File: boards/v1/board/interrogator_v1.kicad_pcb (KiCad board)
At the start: 2 copper layers, 67.9 x 39.9 mm, 330 parts

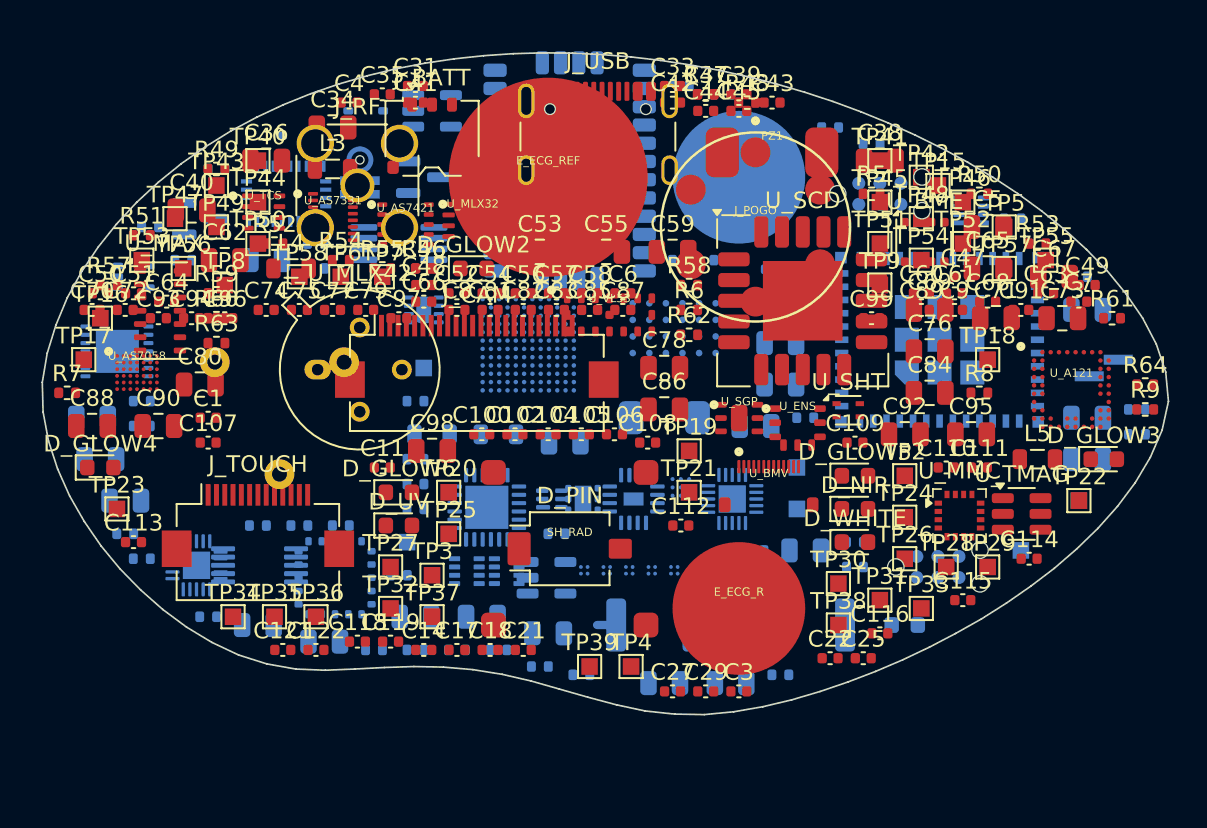
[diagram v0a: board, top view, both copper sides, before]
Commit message: H3.1R/H3.2R: board-first minimal floorplan (ADR-0004) — bean containment removed, board rebuilt placement-true
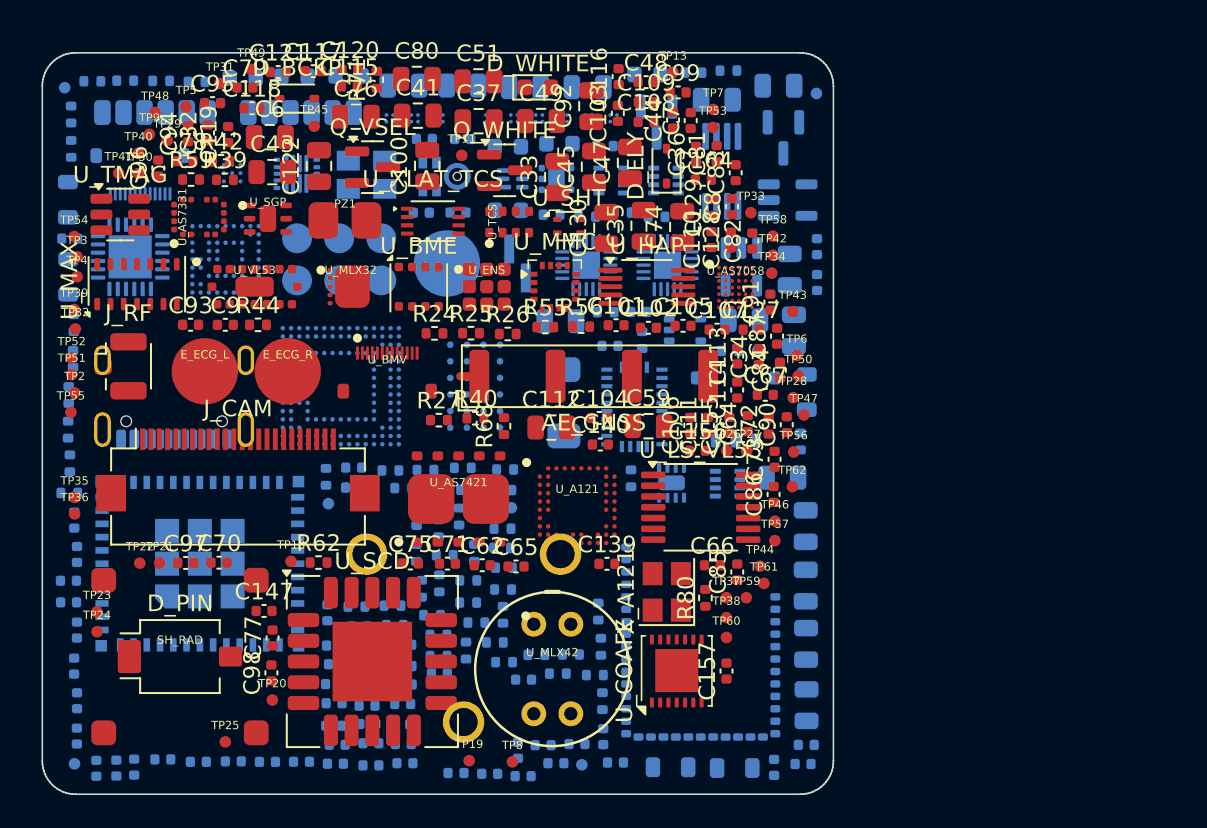
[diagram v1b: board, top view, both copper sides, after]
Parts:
- removed D_NIR: LED_0603_1608Metric, LED_0603_1608Metric
- removed the E_ECG_L at (42.0, 7.50)
- removed the E_ECG_R at (42.0, 33.5)
- removed the E_ECG_REF at (30.5, 7.50)
- removed the J_POGO at (43.0, 10.5)
- removed the J_RF at (19.0, 8.00)
- removed the J_SWD_BL at (50.5, 8.50)
- removed the J_TOUCH at (13.0, 28.5)
- removed the U_CHG at (35.6, 26.9)
- added C124: C_0402_1005Metric, C_0402_1005Metric, B.Cu at (19.1, 34.6)
- added C125: C_0402_1005Metric, C_0402_1005Metric, B.Cu at (21.8, 35.7)
- added C126: C_0402_1005Metric, C_0402_1005Metric, B.Cu at (19.7, 35.6)
- added C127: C_0402_1005Metric, C_0402_1005Metric, F.Cu at (42.7, 16.7)
- added C128: C_0402_1005Metric, C_0402_1005Metric, F.Cu at (41.5, 11.3)
- added C129: C_0402_1005Metric, C_0402_1005Metric, F.Cu at (40.4, 9.33)
- added C130: C_0805_2012Metric, C_0805_2012Metric, F.Cu at (34.0, 10.6)
- added C131: C_0402_1005Metric, C_0402_1005Metric, B.Cu at (21.8, 37.0)
- added C132: C_0402_1005Metric, C_0402_1005Metric, B.Cu at (23.9, 37.4)
- added C133: C_0805_2012Metric, C_0805_2012Metric, B.Cu at (31.2, 16.2)
- added C134: C_0402_1005Metric, C_0402_1005Metric, B.Cu at (17.6, 35.7)
- added C135: C_0402_1005Metric, C_0402_1005Metric, B.Cu at (19.8, 36.9)
- added C136: C_0402_1005Metric, C_0402_1005Metric, B.Cu at (21.8, 38.1)
- added C137: C_0402_1005Metric, C_0402_1005Metric, B.Cu at (17.7, 36.9)
- added C138: C_0805_2012Metric, C_0805_2012Metric, B.Cu at (29.1, 2.07)
- added C139: C_0402_1005Metric, C_0402_1005Metric, F.Cu at (34.0, 30.8)
- added C140: C_0402_1005Metric, C_0402_1005Metric, F.Cu at (33.6, 23.6)
- added C141: C_0402_1005Metric, C_0402_1005Metric, B.Cu at (1.93, 28.2)
- added C142: C_0805_2012Metric, C_0805_2012Metric, B.Cu at (25.3, 1.97)
- added C143: C_0402_1005Metric, C_0402_1005Metric, B.Cu at (2.09, 30.2)
- added C144: C_0402_1005Metric, C_0402_1005Metric, B.Cu at (19.7, 38.1)
- added C145: C_0402_1005Metric, C_0402_1005Metric, B.Cu at (21.7, 39.3)
- added C146: C_0402_1005Metric, C_0402_1005Metric, B.Cu at (17.6, 38.1)
- added C147: C_0402_1005Metric, C_0402_1005Metric, F.Cu at (13.4, 33.6)
- added C148: C_0402_1005Metric, C_0402_1005Metric, B.Cu at (30.2, 41.7)
- added C149: C_0402_1005Metric, C_0402_1005Metric, B.Cu at (32.2, 41.7)
- added C150: C_0402_1005Metric, C_0402_1005Metric, B.Cu at (19.6, 39.4)
- added C151: C_0402_1005Metric, C_0402_1005Metric, B.Cu at (21.7, 40.5)
- added C152: C_0402_1005Metric, C_0402_1005Metric, B.Cu at (17.6, 39.2)
- added C153: C_0402_1005Metric, C_0402_1005Metric, B.Cu at (34.6, 42.8)
- added C154: C_0402_1005Metric, C_0402_1005Metric, B.Cu at (19.6, 40.5)
- added C155: C_0402_1005Metric, C_0402_1005Metric, F.Cu at (41.4, 22.5)
- added C156: C_0402_1005Metric, C_0402_1005Metric, F.Cu at (39.5, 24.0)
- added C157: C_0402_1005Metric, C_0402_1005Metric, F.Cu at (41.3, 37.3)
- added C158: C_0402_1005Metric, C_0402_1005Metric, B.Cu at (28.7, 42.1)
- added C159: C_0402_1005Metric, C_0402_1005Metric, B.Cu at (46.7, 13.8)
- added C160: C_0402_1005Metric, C_0402_1005Metric, B.Cu at (31.0, 42.8)
- added C161: C_0402_1005Metric, C_0402_1005Metric, B.Cu at (21.8, 41.7)
- added C162: C_0402_1005Metric, C_0402_1005Metric, B.Cu at (17.6, 40.6)
- added C163: C_0402_1005Metric, C_0402_1005Metric, B.Cu at (46.7, 11.7)
- added C164: C_0402_1005Metric, C_0402_1005Metric, F.Cu at (39.9, 7.65)
- added E_ECG_L: ELECTRODE_LAND_4MM, ELECTRODE_LAND_4MM, F.Cu at (9.80, 19.2)
- added E_ECG_R: ELECTRODE_LAND_4MM, ELECTRODE_LAND_4MM, F.Cu at (14.8, 19.2)
- added E_ECG_REF: ELECTRODE_LAND_4MM, ELECTRODE_LAND_4MM, B.Cu at (24.4, 12.7)
- added J_POGO: POGO6_COMPACT, POGO6_COMPACT, B.Cu at (17.9, 12.4)
- added J_RF: U.FL_Hirose_U.FL-R-SMT-1_Vertical, U.FL_Hirose_U.FL-R-SMT-1_Vertical, F.Cu at (4.72, 18.9)
- added J_SWD_BL: SWD_PADROW_6, SWD_PADROW_6, B.Cu at (15.6, 3.60)
- added J_TOUCH: ZIF13_MOLEX_503566, ZIF13_MOLEX_503566, B.Cu at (5.90, 7.10)
- added Q_VSEL: SOT-23, SOT-23, F.Cu at (19.9, 6.89)
- added R65: R_0402_1005Metric, R_0402_1005Metric, B.Cu at (33.7, 35.8)
- added R66: R_0402_1005Metric, R_0402_1005Metric, B.Cu at (31.9, 36.3)
- added R67: R_0402_1005Metric, R_0402_1005Metric, B.Cu at (29.8, 36.3)
- added R68: R_0402_1005Metric, R_0402_1005Metric, F.Cu at (27.8, 22.5)
- added R69: R_0402_1005Metric, R_0402_1005Metric, B.Cu at (3.02, 1.71)
- added R70: R_0402_1005Metric, R_0402_1005Metric, B.Cu at (33.3, 37.5)
- added R71: R_0402_1005Metric, R_0402_1005Metric, F.Cu at (20.2, 1.62)
- added R72: R_0402_1005Metric, R_0402_1005Metric, B.Cu at (18.9, 33.4)
- added R73: R_0402_1005Metric, R_0402_1005Metric, B.Cu at (27.3, 35.5)
- added R74: R_0402_1005Metric, R_0402_1005Metric, B.Cu at (31.1, 37.4)
- added R75: R_0402_1005Metric, R_0402_1005Metric, B.Cu at (23.9, 35.1)
- added R76: R_0402_1005Metric, R_0402_1005Metric, B.Cu at (27.8, 36.7)
- added R77: R_0402_1005Metric, R_0402_1005Metric, B.Cu at (21.3, 34.5)
- added R78: R_0402_1005Metric, R_0402_1005Metric, B.Cu at (35.5, 25.7)
- added R79: R_0402_1005Metric, R_0402_1005Metric, B.Cu at (33.8, 39.1)
- added R80: R_0402_1005Metric, R_0402_1005Metric, F.Cu at (40.0, 32.9)
- added R81: R_0402_1005Metric, R_0402_1005Metric, B.Cu at (25.5, 36.0)
- added R82: R_0402_1005Metric, R_0402_1005Metric, B.Cu at (23.9, 36.4)
- added TP59: TESTPOINT_PAD_0.8MM, TESTPOINT_PAD_0.8MM, F.Cu at (42.5, 32.9)
- added TP60: TESTPOINT_PAD_0.8MM, TESTPOINT_PAD_0.8MM, F.Cu at (41.2, 35.2)
- added TP61: TESTPOINT_PAD_0.8MM, TESTPOINT_PAD_0.8MM, F.Cu at (43.5, 32.0)
- added TP62: TESTPOINT_PAD_0.8MM, TESTPOINT_PAD_0.8MM, F.Cu at (45.2, 26.2)
- added U_CHG: BQ25620_WQFN18_RYK, BQ25620_WQFN18_RYK, B.Cu at (15.3, 7.30)
- added U_LS_VL53: TSSOP-14_4.4x5mm_P0.65mm, TSSOP-14_4.4x5mm_P0.65mm, F.Cu at (39.7, 27.4)
- added U_SW1V8_AIR: TPS22916_CSP4, TPS22916_CSP4, B.Cu at (34.5, 3.95)
- added U_SW1V8_OPTICAL: TPS22916_CSP4, TPS22916_CSP4, B.Cu at (31.4, 3.95)
- added U_SW1V8_RADAR: TPS22916_CSP4, TPS22916_CSP4, B.Cu at (33.0, 3.95)
- added U_XLAT_TCS: VSSOP-8_2.4x2.1mm_P0.5mm, VSSOP-8_2.4x2.1mm_P0.5mm, F.Cu at (23.6, 10.1)
- added X_A121: Crystal_SMD_3225-4Pin_3.2x2.5mm, Crystal_SMD_3225-4Pin_3.2x2.5mm, F.Cu at (37.7, 32.5)
- added X_HSE: Crystal_SMD_3225-4Pin_3.2x2.5mm, Crystal_SMD_3225-4Pin_3.2x2.5mm, B.Cu at (19.5, 7.35)
- AE_GNSS, D_BCKP, D_FLY, Q_WHITE, R24, R25, R26, R27, R39, R40, R42, R44, U_COAFE, U_HAP: moved to F.Cu
- C1, C11, C14, C22, C27, C3, C4, C42, C46, C50, C52, C54, C56, C57, C58, C60, C61, C63, C68, C89, D_GLOW2, D_GLOW3, D_GLOW4, D_GLOW5, D_GLOW6, D_UV, J_BATT, J_USB, L3, L4, L5, R47, R48, R49, R5, R50, R51, R52, R53, R54, R57, R58, R6, R60, R61, R63, R64, R7, R8, R9: moved to B.Cu
- C100, C112, C122, C33, C35, C37, C41, C43, C45, C47, C49, C51, C6, C74: value C_0402_1005Metric -> C_0805_2012Metric; footprint C_0402_1005Metric -> C_0805_2012Metric
- C101, C103, C117, C120, C32: value C_0805_2012Metric -> C_0402_1005Metric; footprint C_0805_2012Metric -> C_0402_1005Metric; moved to F.Cu
- C12, C123, C13, C16, C19, C2, C23, C26, C30, C34, C36, C62, C65, C67, C71, C73, C78, C84, C86, C90, C95, C98: value C_0805_2012Metric -> C_0402_1005Metric; footprint C_0805_2012Metric -> C_0402_1005Metric
- C17, C18, C21, C25, C29, C31, C39: value C_0402_1005Metric -> C_0805_2012Metric; footprint C_0402_1005Metric -> C_0805_2012Metric; moved to B.Cu
- C38, C40, C5, C53, C55, C69, C88: value C_0805_2012Metric -> C_0402_1005Metric; footprint C_0805_2012Metric -> C_0402_1005Metric; moved to B.Cu
- J_SWD_N6: value Tag-Connect_TC2030-IDC-NL_2x03_P1.27mm_Vertical -> SWD_PADROW_6; footprint Tag-Connect_TC2030-IDC-NL_2x03_P1.27mm_Vertical -> SWD_PADROW_6
- TP1, TP10, TP12, TP14, TP18, TP19, TP2, TP20, TP21, TP22, TP23, TP24, TP25, TP26, TP27, TP28, TP29, TP3, TP30, TP31, TP32, TP33, TP34, TP35, TP36, TP37, TP38, TP39, TP4, TP40, TP41, TP42, TP43, TP44, TP45, TP46, TP47, TP48, TP49, TP5, TP50, TP51, TP52, TP53, TP54, TP55, TP56, TP57, TP58, TP6, TP7, TP8, TP9: value TestPoint_Pad_1.0x1.0mm -> TESTPOINT_PAD_0.8MM; footprint TestPoint_Pad_1.0x1.0mm -> TESTPOINT_PAD_0.8MM
- TP11, TP13: value TestPoint_Pad_1.0x1.0mm -> TESTPOINT_PAD_0.8MM; footprint TestPoint_Pad_1.0x1.0mm -> TESTPOINT_PAD_0.8MM; moved to F.Cu
- TP15, TP16, TP17: value TestPoint_Pad_1.0x1.0mm -> TESTPOINT_PAD_0.8MM; footprint TestPoint_Pad_1.0x1.0mm -> TESTPOINT_PAD_0.8MM; moved to B.Cu
- U_MLX32: value MLX90632_SFN8_3x3 -> MLX90632_SFN5_3x3; footprint MLX90632_SFN8_3x3 -> MLX90632_SFN5_3x3
- U_MLX42: value TO-39-4 -> MLX90642_TO39; footprint TO-39-4 -> MLX90642_TO39
- U_N657: value ST_VFBGA142_PLACEHOLDER -> ST_VFBGA142; footprint ST_VFBGA142_PLACEHOLDER -> ST_VFBGA142
- moved R9 65.1 mm to (1.63, 26.5)
- moved R61 63.3 mm to (1.56, 22.7), turned to -90 degrees
- moved C16 61.9 mm to (1.58, 31.8)
- moved TP55 59.5 mm to (1.72, 21.7)
- moved L5 59.5 mm to (1.56, 13.5), turned to -90 degrees
- moved C61 59.1 mm to (3.26, 43.1), turned to -90 degrees
- moved R53 59.1 mm to (1.59, 20.6), turned to -90 degrees
- moved TP14 58.5 mm to (1.94, 42.9)
- moved C60 57.5 mm to (2.08, 41.2), turned to -90 degrees
- moved C5 57.5 mm to (9.41, 42.7)
- moved U_TMAG 57.3 mm to (4.70, 9.75)
- moved TP22 56.7 mm to (5.88, 30.8)
- moved TP29 55.8 mm to (7.53, 5.28)
- moved R8 55.0 mm to (1.66, 24.7), turned to -90 degrees
- moved J_SWD_N6 54.6 mm to (6.80, 3.60)
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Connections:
- C1 pad 1: VBUS_C -> PD_VDDD
- C10 pad 1: VSYS -> N$8
- C100 pad 1: 3V3_RADAR -> 3V3_CONTACT
- C101 pad 1: 3V3_RADAR -> 3V3_CONTACT
- C102 pad 1: 3V3_GNSS -> 3V3_CONTACT
- C103 pad 1: 3V3_GNSS -> 3V3_CONTACT
- C104 pad 1: GNSS_VBCKP -> 3V3_AIR
- C105 pad 1: 3V3_SYS -> 3V3_AIR
- C106 pad 1: 3V3_AON -> 3V3_AIR
- C107 pad 1: 3V3_AON -> 3V3_AIR
- C108 pad 1: PIN_BIAS -> 1V8_AIR
- C109 pad 1: RAD_VREF -> 1V8_AIR
- C11 pad 1: VBAT -> N$9
- C110 pad 1: RAD_IN -> 3V3_AIR
- C110 pad 2: RAD_ANALOG -> GND
- C111 pad 1: 3V3_SYS -> 3V3_AIR
- C112 pad 1: 3V3_SYS -> 3V3_AIR
- C113 pad 1: RF_IN -> 3V3_AIR
- C113 pad 2: N$24 -> GND
- C114 pad 1: N$25 -> 3V3_AIR
- C115 pad 1: 3V3_SYS -> 1V8_OPTICAL
- C116 pad 1: 3V3_AIR -> 1V8_OPTICAL
- C117 pad 1: 3V3_AIR -> 3V3_OPTICAL
- C118 pad 1: N$29 -> 3V3_OPTICAL
- C118 pad 2: N$30 -> GND
- C119 pad 1: 3V3_AON -> 3V3_OPTICAL
- C12 pad 1: VBAT -> N$11
- C12 pad 2: GND -> N$10
- C120 pad 1: 3V3_AON -> 3V3_OPTICAL
- C121 pad 1: N$31 -> 3V3_OPTICAL
- C122 pad 1: 3V3_AON -> 3V3_OPTICAL
- C123 pad 1: 3V3_AON -> 3V3_SYS
- C14 pad 1: 3V3_AON -> VSYS
- C15 pad 1: 3V3_AON -> VSYS
- C16 pad 1: VSYS -> VBAT
- C17 pad 1: VDD_CORE_N6 -> VBAT
- C18 pad 1: VDD_CORE_N6 -> VSYS
- C19 pad 1: VDD_CORE_N6 -> 3V3_AON
- C2 pad 1: VBUS_C -> PD_VDDD
- C20 pad 1: VSYS -> 3V3_AON
- C21 pad 1: 3V3_SYS -> VSYS
- C22 pad 1: 3V3_SYS -> VDD_CORE_N6
- C23 pad 1: 3V3_SYS -> VDD_CORE_N6
- C24 pad 1: VSYS -> VDD_CORE_N6
- C25 pad 1: 1V8 -> VSYS
- C26 pad 1: 1V8 -> 3V3_SYS
- C27 pad 1: 3V3_OPTICAL -> 3V3_SYS
- C28 pad 1: 3V3_OPTICAL -> 3V3_SYS
- C29 pad 1: 3V3_AIR -> VSYS
- C3 pad 1: PROT_VDD -> PD_VDDD
- C3 pad 2: CELL_N -> GND
- C30 pad 1: 3V3_AIR -> 1V8
- C31 pad 1: 3V3_CONTACT -> 1V8
- C32 pad 1: 3V3_CONTACT -> 3V3_OPTICAL
- C33 pad 1: 3V3_RADAR -> 3V3_OPTICAL
- C34 pad 1: 3V3_RADAR -> 3V3_AIR
- C35 pad 1: 3V3_GNSS -> 3V3_AIR
- C36 pad 1: 3V3_GNSS -> 3V3_CONTACT
- C37 pad 1: 3V3_WIFI -> 3V3_CONTACT
- C38 pad 1: 3V3_WIFI -> 3V3_RADAR
- C39 pad 1: VACC -> 3V3_RADAR
- C4 pad 1: 3V3_AON -> N$1
- C40 pad 1: VACC -> 3V3_GNSS
- C41 pad 1: VDD_CORE_N6 -> 3V3_GNSS
- C42 pad 1: VDD_CORE_N6 -> 3V3_WIFI
- C43 pad 1: 1V8 -> 3V3_WIFI
- C44 pad 1: 1V8 -> 1V8_OPTICAL
- C45 pad 1: 3V3_SYS -> 1V8_OPTICAL
- C46 pad 1: 3V3_SYS -> 1V8_RADAR
- C47 pad 1: 3V3_SYS -> 1V8_RADAR
- C48 pad 1: 3V3_SYS -> 1V8_AIR
- C49 pad 1: 1V8 -> 1V8_AIR
- C5 pad 1: N$8 -> VBUS_C
- C50 pad 1: 1V8 -> VACC
- C51 pad 1: 3V3_AON -> VACC
- C52 pad 1: 3V3_AON -> N6_V08CAP
- C54 pad 1: 3V3_WIFI -> 1V8
- C55 pad 1: 3V3_WIFI -> VDD_CORE_N6
- C56 pad 1: C6_EN -> VDD_CORE_N6
- C57 pad 1: 3V3_OPTICAL -> VDD_CORE_N6
- C58 pad 1: 3V3_OPTICAL -> VDD_CORE_N6
- C59 pad 1: 3V3_OPTICAL -> VDD_CORE_N6
- C6 pad 1: N$9 -> VBUS_C
- C60 pad 1: 3V3_SYS -> 1V8
- C61 pad 1: 3V3_SYS -> 1V8
- C62 pad 1: 3V3_SYS -> 1V8
- C63 pad 1: 3V3_SYS -> 1V8
- C66 pad 1: 3V3_OPTICAL -> 3V3_SYS
- C67 pad 1: 3V3_OPTICAL -> 3V3_SYS
- C68 pad 1: 3V3_OPTICAL -> N6_OSC_IN
- C69 pad 1: 3V3_OPTICAL -> N6_OSC_OUT
- C7 pad 1: N$11 -> PROT_VDD
- C7 pad 2: N$10 -> CELL_N
- C72 pad 1: 3V3_CONTACT -> 3V3_AON
- C73 pad 1: 3V3_CONTACT -> 3V3_AON
- C74 pad 1: 3V3_CONTACT -> 3V3_AON
- C75 pad 1: 3V3_CONTACT -> 3V3_WIFI
- C76 pad 1: 3V3_CONTACT -> 3V3_WIFI
- C77 pad 1: 3V3_AIR -> C6_EN
- C78 pad 1: 3V3_AIR -> 3V3_OPTICAL
- C79 pad 1: 3V3_AIR -> 3V3_OPTICAL
- C8 pad 1: VSYS -> PACKP
- C80 pad 1: 3V3_AIR -> 3V3_OPTICAL
- C81 pad 1: 1V8 -> 1V8_OPTICAL
- C82 pad 1: 3V3_AIR -> 1V8_OPTICAL
- C83 pad 1: 3V3_AIR -> 1V8_OPTICAL
- C84 pad 1: 3V3_AIR -> 3V3_SYS
- C85 pad 1: 3V3_AIR -> 3V3_SYS
- C86 pad 1: 3V3_AIR -> 3V3_SYS
- C87 pad 1: 3V3_OPTICAL -> 3V3_SYS
- C88 pad 1: 3V3_OPTICAL -> BNO_CAP
- C89 pad 1: 3V3_OPTICAL -> ADS_CAP
- C9 pad 1: VSYS -> GAUGE_VDD
- C90 pad 1: 3V3_OPTICAL -> 3V3_SYS
- C91 pad 1: 3V3_OPTICAL -> 3V3_SYS
- C92 pad 1: 3V3_OPTICAL -> 3V3_SYS
- C93 pad 1: 3V3_SYS -> 3V3_OPTICAL
- C94 pad 1: 3V3_SYS -> 3V3_OPTICAL
- C95 pad 1: 3V3_SYS -> 3V3_OPTICAL
- C96 pad 1: 3V3_SYS -> 3V3_OPTICAL
- C97 pad 1: 3V3_AIR -> 1V8
- C98 pad 1: 3V3_AIR -> 1V8
- C99 pad 1: 3V3_RADAR -> 3V3_CONTACT
- J_BATT pad 1: VBAT -> PACKP
- J_BATT pad MP: (no net) -> GND
- J_CAM pad MP: (no net) -> GND
- L2 pad 1: N$15 -> N$16
- L3 pad 1: N$16 -> N$17
- L4 pad 1: N$18 -> N$19
- L5 pad 1: N$20 -> N$21
- Q_FAN pad 1: N$28 -> N$31
- Q_PROT pad 2: N$5 -> N$4
- Q_PROT pad 5: N$6 -> N$5
- Q_UV pad 1: N$26 -> N$29
- Q_WHITE pad 1: N$27 -> N$30
- R1 pad 1: N$1 -> PD_VDDD
- R1 pad 2: GND -> N$2
- R10 pad 1: BATT_NTC -> N$9
- R10 pad 2: GND -> BATT_NTC
- R11 pad 1: VDD_CORE_N6 -> BATT_NTC
- R11 pad 2: N$17 -> GND
- R12 pad 1: N$17 -> N$15
- R13 pad 1: 3V3_SYS -> VDD_CORE_N6
- R13 pad 2: N$19 -> N$18
- R14 pad 1: N$19 -> N$18
- R15 pad 1: 1V8 -> N$18
- R15 pad 2: N$21 -> VSEL_LEG
- R16 pad 1: N$21 -> N6_VCORE_SEL
- R17 pad 1: I2CA_SDA -> 3V3_SYS
- R17 pad 2: 3V3_SYS -> N$20
- R18 pad 1: I2CA_SCL -> N$20
- R18 pad 2: 3V3_SYS -> GND
- R19 pad 1: I2CB_SDA -> 1V8
- R19 pad 2: 3V3_SYS -> N$22
- R20 pad 1: I2CB_SCL -> N$22
- R20 pad 2: 3V3_SYS -> GND
- R21 pad 1: N6_NRST -> N6_PWR_ON
- R21 pad 2: 3V3_SYS -> GND
- R22 pad 1: N6_BOOT0 -> N$23
- R23 pad 1: NOR_RST_N -> N$24
- R23 pad 2: 1V8 -> GND
- R24 pad 1: SENT_SDA -> I2CA_SDA
- R24 pad 2: 3V3_AON -> 3V3_SYS
- R25 pad 1: SENT_SCL -> I2CA_SCL
- R25 pad 2: 3V3_AON -> 3V3_SYS
- R26 pad 1: GAUGE_INT_N -> I2CB_SDA
- R26 pad 2: 3V3_AON -> 3V3_SYS
- R27 pad 1: CHG_INT_N -> I2CB_SCL
- R27 pad 2: 3V3_AON -> 3V3_SYS
- R28 pad 1: PD_FAULT_N -> N6_NRST
- R28 pad 2: 3V3_AON -> 3V3_SYS
- R29 pad 1: BL_RESET_N -> N6_BOOT0
- R29 pad 2: 3V3_AON -> GND
- R3 pad 1: N$3 -> PD_VDDD
- R3 pad 2: GND -> N$3
- R30 pad 1: 3V3_WIFI -> N6_BOOT1
- R30 pad 2: C6_EN -> GND
- R31 pad 1: C6_BOOT -> NOR_RST_N
- R31 pad 2: 3V3_WIFI -> 1V8
- R32 pad 1: INT_VL53 -> SENT_SDA
- R32 pad 2: 3V3_SYS -> 3V3_AON
- R33 pad 1: BNO_PS0_WAKE -> SENT_SCL
- R33 pad 2: 3V3_SYS -> 3V3_AON
- R34 pad 1: INT_BNO -> GAUGE_INT_N
- R34 pad 2: 3V3_SYS -> 3V3_AON
- R35 pad 1: N$22 -> CHG_INT_N
- R35 pad 2: 3V3_SYS -> 3V3_AON
- R36 pad 1: N$23 -> BL_RESET_N
- R36 pad 2: 3V3_SYS -> 3V3_AON
- R37 pad 1: PIEZO_P -> 3V3_WIFI
- R37 pad 2: GND -> C6_EN
- R38 pad 1: PIEZO_N -> C6_BOOT
- R38 pad 2: GND -> 3V3_WIFI
- R39 pad 1: INT_MAX -> VL53_SPI_SEL
- R39 pad 2: 3V3_SYS -> 1V8_OPTICAL
- R4 pad 1: N$4 -> N$3
- R40 pad 1: INT_ENS -> VL53_NCS_1V8
- R40 pad 2: 3V3_SYS -> 1V8_OPTICAL
- R41 pad 1: INT_TCS -> CS_VL53_N
- R42 pad 1: INT_AS7421 -> VL53_GPIO2
- R42 pad 2: 3V3_SYS -> 1V8_OPTICAL
- R43 pad 1: 3V3_OPTICAL -> LPN_VL53
- R43 pad 2: NIR_LED_A -> GND
- R44 pad 1: INT_TMAG -> INT_VL53
- R44 pad 2: 3V3_SYS -> 1V8_OPTICAL
- R45 pad 1: 3V3_AON -> BNO_PS0_WAKE
- R45 pad 2: PIN_BIAS -> 3V3_SYS
- R46 pad 1: 3V3_AON -> INT_BNO
- R46 pad 2: RAD_VREF -> 3V3_SYS
- R47 pad 1: RAD_VREF -> N$25
- R47 pad 2: GND -> 3V3_SYS
- R48 pad 1: RAD_IN -> BNO_ENV_SCL
- R48 pad 2: RAD_ANALOG -> 3V3_SYS
- R49 pad 1: 3V3_AON -> BNO_ENV_SDA
- R49 pad 2: RAD_VTH -> 3V3_SYS
- R5 pad 1: VBAT -> PACKP
- R50 pad 1: RAD_VTH -> N$26
- R50 pad 2: GND -> 3V3_SYS
- R51 pad 1: SHIELD_RAD -> PIEZO_P
- R52 pad 1: 3V3_OPTICAL -> PIEZO_N
- R52 pad 2: UV_LED_A -> GND
- R53 pad 1: UV_GATE -> INT_MAX
- R53 pad 2: N$26 -> 3V3_SYS
- R54 pad 1: 3V3_OPTICAL -> INT_ENS
- R54 pad 2: WHITE_LED_A -> 3V3_SYS
- R55 pad 1: EN_WHITE -> I2CA_SDA_1V8
- R55 pad 2: N$27 -> 1V8_OPTICAL
- R56 pad 1: GLOW1 -> I2CA_SCL_1V8
- R56 pad 2: GLOW1_A -> 1V8_OPTICAL
- R57 pad 1: GLOW2 -> EN_OPTICAL
- R57 pad 2: GLOW2_A -> 3V3_SYS
- R58 pad 1: GLOW3 -> INT_TCS
- R58 pad 2: GLOW3_A -> 3V3_SYS
- R59 pad 1: GLOW4 -> AS7331_REXT
- R59 pad 2: GLOW4_A -> GND
- R6 pad 1: N$7 -> N$6
- R60 pad 1: GLOW5 -> INT_AS7421
- R60 pad 2: GLOW5_A -> 3V3_SYS
- R61 pad 1: GLOW6 -> INT_TMAG
- R61 pad 2: GLOW6_A -> 3V3_SYS
- R62 pad 1: EN_FAN -> 3V3_AON
- R62 pad 2: N$28 -> PIN_BIAS
- R63 pad 1: TOUCH_RDY_N -> 3V3_AON
- R63 pad 2: 3V3_AON -> RAD_VREF
- R64 pad 1: TOUCH_MCLR_N -> RAD_VREF
- R64 pad 2: 3V3_AON -> GND
- R7 pad 1: N$12 (its old number) -> N$7
- R8 pad 2: VBAT -> GND
- R9 pad 1: N$9 -> N$13
- R9 pad 2: BATT_NTC -> VBAT
- TP11 pad 1: VBUS_C -> 1V8_OPTICAL
- TP12 pad 1: VBAT -> 1V8_RADAR
- TP13 pad 1: VSYS -> 1V8_AIR
- TP14 pad 1: 3V3_AON -> VBUS_C
- TP15 pad 1: 3V3_SYS -> VBAT
- TP16 pad 1: VDD_CORE_N6 -> VSYS
- TP17 pad 1: 1V8 -> 3V3_AON
- TP18 pad 1: N6_BOOT0 -> 3V3_SYS
- TP19 pad 1: C6_TXD0 -> VDD_CORE_N6
- TP20 pad 1: C6_RXD0 -> 1V8
- TP21 pad 1: C6_BOOT -> N6_BOOT0
- TP22 pad 1: SPI1_SCK -> N6_BOOT1
- TP23 pad 1: SPI1_MISO -> C6_TXD0
- TP24 pad 1: SPI1_MOSI -> C6_RXD0
- TP25 pad 1: I2CA_SDA -> C6_BOOT
- TP26 pad 1: I2CA_SCL -> SPI1_SCK
- TP27 pad 1: I2CB_SDA -> SPI1_MISO
- TP28 pad 1: I2CB_SCL -> SPI1_MOSI
- TP29 pad 1: SENT_SDA -> I2CA_SDA
- TP3 pad 1: PD_FAULT_N -> PD_FAULT
- TP30 pad 1: SENT_SCL -> I2CA_SCL
- TP31 pad 1: SDIO_CLK -> I2CB_SDA
- TP32 pad 1: SDIO_CMD -> I2CB_SCL
- TP33 pad 1: IMCU_N6_TX -> SENT_SDA
- TP34 pad 1: IMCU_N6_RX -> SENT_SCL
- TP35 pad 1: GNSS_PPS -> SDIO_CLK
- TP36 pad 1: N6_SWDIO -> SDIO_CMD
- TP37 pad 1: N6_SWCLK -> IMCU_N6_TX
- TP38 pad 1: BL_SWDIO -> IMCU_N6_RX
- TP39 pad 1: BL_SWCLK -> GNSS_PPS
- TP40 pad 1: BNO_PS0_WAKE -> N6_SWDIO
- TP41 pad 1: ACC_AN2 -> N6_SWCLK
- TP42 pad 1: CO_AFE_OUT -> BL_SWDIO
- TP43 pad 1: GEIGER_PULSE -> BL_SWCLK
- TP44 pad 1: N6_SWO -> BNO_PS0_WAKE
- TP45 pad 1: BL_SWO -> ACC_AN2
- TP46 pad 1: GND -> CO_AFE_OUT
- TP47 pad 1: USB_DP -> GEIGER_PULSE
- TP48 pad 1: USB_DM -> N6_SWO
- TP49 pad 1: ACC_AN1 -> BL_SWO
- TP50 pad 1: GNSS_TX -> GND
- TP51 pad 1: GNSS_RX -> USB_DP
- TP52 pad 1: RAD_ANALOG -> USB_DM
- TP53 pad 1: RF_DET_OUT -> ACC_AN1
- TP54 pad 1: CLK_ADS -> GNSS_TX
- TP55 pad 1: WAKE_N6 -> GNSS_RX
- TP56 pad 1: ATTN_N6 -> RAD_ANALOG
- TP57 pad 1: EN_N6 -> RF_DET_OUT
- TP58 pad 1: INTERLOCK_OK -> CLK_ADS
- U_1V8 pad 1: EN_N6 -> 3V3_SYS
- U_1V8 pad 3: VSYS -> N$21
- U_1V8 pad 4: N$21 -> VSYS
- U_1V8 pad 5: N$20 -> N$22
- U_A121 pad A2: (no net) -> GND
- U_A121 pad A3: (no net) -> GND
- U_A121 pad A4: (no net) -> GND
- U_A121 pad A5: (no net) -> GND
- U_A121 pad A6: (no net) -> GND
- U_A121 pad A7: (no net) -> GND
- U_A121 pad A8: (no net) -> GND
- U_A121 pad A9: (no net) -> GND
- U_A121 pad B1: (no net) -> GND
- U_A121 pad B10: (no net) -> GND
- U_A121 pad B2: (no net) -> GND
- U_A121 pad B9: (no net) -> GND
- U_A121 pad C1: (no net) -> GND
- U_A121 pad C10: (no net) -> GND
- U_A121 pad C2: (no net) -> 1V8_RADAR
- U_A121 pad C9: (no net) -> 1V8_RADAR
- U_A121 pad D1: (no net) -> 1V8_RADAR
- U_A121 pad D10: (no net) -> 1V8_RADAR
- U_A121 pad D2: (no net) -> GND
- U_A121 pad D9: (no net) -> GND
- U_A121 pad E1: (no net) -> GND
- U_A121 pad E10: (no net) -> GND
- U_A121 pad E2: (no net) -> GND
- U_A121 pad E9: (no net) -> GND
- U_A121 pad F1: (no net) -> GND
- U_A121 pad F10: (no net) -> 3V3_RADAR
- U_A121 pad F2: (no net) -> GND
- U_A121 pad F9: (no net) -> GND
- U_A121 pad G1: (no net) -> GND
- U_A121 pad G10: (no net) -> GND
- U_A121 pad H1: (no net) -> GND
- U_A121 pad H10: (no net) -> A121_XOUT
- U_A121 pad H2: (no net) -> GND
- U_A121 pad H9: (no net) -> GND
- U_A121 pad J1: (no net) -> 3V3_RADAR
- U_A121 pad J10: (no net) -> A121_XIN
- U_A121 pad J2: (no net) -> CS_A121_N
- U_A121 pad J3: (no net) -> GND
- U_A121 pad J5: (no net) -> GND
- U_A121 pad J6: (no net) -> GND
- U_A121 pad J8: (no net) -> GND
- U_A121 pad J9: (no net) -> 1V8_RADAR
- U_A121 pad K2: (no net) -> SPI1_SCK
- U_A121 pad K3: (no net) -> SPI1_MISO
- U_A121 pad K4: (no net) -> GND
- U_A121 pad K5: (no net) -> GND
- U_A121 pad K6: (no net) -> SPI1_MOSI
- U_A121 pad K7: (no net) -> GND
- U_A121 pad K8: (no net) -> IRQ_A121
- U_A121 pad K9: (no net) -> 3V3_RADAR
- U_ADS pad 1: 3V3_SYS -> PIEZO_P
- U_ADS pad 10: GND -> CS_ADS_N
- U_ADS pad 11: CO_AFE_OUT -> DRDY_ADS
- U_ADS pad 12: GND -> SPI1_SCK
- U_ADS pad 13: SPI1_SCK -> SPI1_MISO
- U_ADS pad 15: SPI1_MISO -> CLK_ADS
- U_ADS pad 16: CS_ADS_N -> ADS_CAP
- U_ADS pad 17: DRDY_ADS -> GND
- U_ADS pad 18: N$23 -> 3V3_SYS
- U_ADS pad 19: CLK_ADS -> 3V3_SYS
- U_ADS pad 2: 3V3_SYS -> PIEZO_N
- U_ADS pad 20: (no net) -> GND
- U_ADS pad 21: (no net) -> GND
- U_ADS pad 4: GND -> RAD_ANALOG
- U_ADS pad 5: PIEZO_P -> ACC_AN2
- U_ADS pad 6: PIEZO_N -> GND
- U_ADS pad 7: RAD_ANALOG -> GND
- U_ADS pad 8: GND -> CO_AFE_OUT
- U_ADS pad 9: ACC_AN2 -> N$26
- U_AON pad 1: VSYS -> GND
- U_AON pad 2: GND -> VSYS
- U_AON pad 3: VSYS -> GND
- U_AON pad 4: N$15 -> VSYS
- U_AON pad 5: 3V3_AON -> N$15
- U_AON pad 7: (no net) -> N$16
- U_AON pad 8: (no net) -> 3V3_AON
- U_AS7331 pad 1: 3V3_OPTICAL -> GND
- U_AS7331 pad 10: (no net) -> 3V3_OPTICAL
- U_AS7331 pad 11: (no net) -> GND
- U_AS7331 pad 12: (no net) -> I2CB_SDA
- U_AS7331 pad 13: (no net) -> I2CB_SCL
- U_AS7331 pad 14: (no net) -> GND
- U_AS7331 pad 15: (no net) -> GND
- U_AS7331 pad 16: (no net) -> GND
- U_AS7331 pad 3: I2CB_SDA -> 3V3_OPTICAL
- U_AS7331 pad 4: I2CB_SCL -> AS7331_REXT
- U_AS7331 pad 7: RDY_AS7331 -> GND
- U_AS7331 pad 9: (no net) -> RDY_AS7331
- U_AS7421 pad 1: 3V3_OPTICAL -> INT_AS7421
- U_AS7421 pad 10: (no net) -> I2CB_SCL
- U_AS7421 pad 2: GND -> 3V3_OPTICAL
- U_AS7421 pad 3: I2CB_SDA -> GND
- U_AS7421 pad 4: I2CB_SCL -> GND
- U_AS7421 pad 5: INT_AS7421 -> GND
- U_AS7421 pad 6: NIR_LED_K -> 3V3_OPTICAL
- U_AS7421 pad 7: (no net) -> GND
- U_AS7421 pad 8: (no net) -> GND
- U_AS7421 pad 9: (no net) -> I2CB_SDA
- U_BL54 pad 1: 3V3_AON -> GND
- U_BL54 pad 10: EN_GNSS -> SENT_SCL
- U_BL54 pad 11: EN_WIFI -> GLOW3
- U_BL54 pad 12: EN_N6 -> GLOW4
- U_BL54 pad 13: EN_FAN -> CHG_INT_N
- U_BL54 pad 14: EN_ACC -> (no net)
- U_BL54 pad 15: EN_HAPTIC -> (no net)
- U_BL54 pad 16: INTERLOCK_OK -> GND
- U_BL54 pad 17: IMCU_N6_RX -> WAKE_N6
- U_BL54 pad 18: IMCU_N6_TX -> ATTN_N6
- U_BL54 pad 19: WAKE_N6 -> TOUCH_RDY_N
- U_BL54 pad 2: GND -> GLOW1
- U_BL54 pad 20: ATTN_N6 -> EN_OPTICAL
- U_BL54 pad 21: TOUCH_RDY_N -> EN_AIR
- U_BL54 pad 22: GAUGE_INT_N -> EN_CONTACT
- U_BL54 pad 23: CHG_INT_N -> EN_RADAR
- U_BL54 pad 24: GLOW1 -> (no net)
- U_BL54 pad 25: GLOW2 -> (no net)
- U_BL54 pad 26: GLOW3 -> 3V3_AON
- U_BL54 pad 27: GLOW4 -> GND
- U_BL54 pad 28: GLOW5 -> EN_GNSS
- U_BL54 pad 29: GLOW6 -> EN_WIFI
- U_BL54 pad 3: SENT_SCL -> IMCU_N6_RX
- U_BL54 pad 30: (no net) -> EN_N6
- U_BL54 pad 31: (no net) -> GEIGER_PULSE
- U_BL54 pad 32: BL_SWDIO -> EN_FAN
- U_BL54 pad 4: SENT_SDA -> IMCU_N6_TX
- U_BL54 pad 5: GEIGER_PULSE -> BL_SWDIO
- U_BL54 pad 6: EN_OPTICAL -> BL_SWCLK
- U_BL54 pad 7: EN_AIR -> BL_RESET_N
- U_BL54 pad 8: EN_CONTACT -> GLOW2
- U_BL54 pad 9: EN_RADAR -> SENT_SDA
- U_BME pad 1: 3V3_AIR -> GND
- U_BME pad 3: GND -> I2CB_SDA
- U_BME pad 5: I2CB_SDA -> 3V3_AIR
- U_BME pad 7: 3V3_AIR -> GND
- U_BME pad 8: (no net) -> 3V3_AIR
- U_BMV pad 10: (no net) -> 3V3_AIR
- U_BMV pad 11: (no net) -> 3V3_AIR
- U_BMV pad 12: (no net) -> INT_BMV
- U_BMV pad 2: 3V3_AIR -> GND
- U_BMV pad 3: GND -> 3V3_AIR
- U_BMV pad 4: I2CB_SDA -> 3V3_AIR
- U_BMV pad 5: I2CB_SCL -> I2CB_SDA
- U_BMV pad 6: INT_BMV -> I2CB_SCL
- U_BMV pad 9: 3V3_AIR -> GND
- U_BMV pad MP1: (no net) -> GND
- U_BMV pad MP2: (no net) -> GND
- U_BNO pad 1: 3V3_SYS -> (no net)
- U_BNO pad 10: INT_BNO -> 3V3_SYS
- U_BNO pad 12: N$22 -> (no net)
- U_BNO pad 14: (no net) -> INT_BNO
- U_BNO pad 15: (no net) -> BNO_ENV_SCL
- U_BNO pad 16: (no net) -> BNO_ENV_SDA
- U_BNO pad 17: (no net) -> SPI1_MOSI
- U_BNO pad 18: (no net) -> CS_BNO_N
- U_BNO pad 19: (no net) -> SPI1_SCK
- U_BNO pad 2: 3V3_SYS -> GND
- U_BNO pad 20: (no net) -> SPI1_MISO
- U_BNO pad 25: (no net) -> GND
- U_BNO pad 28: (no net) -> 3V3_SYS
- U_BNO pad 3: GND -> 3V3_SYS
- U_BNO pad 4: BNO_PS0_WAKE -> N$25
- U_BNO pad 6: CS_BNO_N -> BNO_PS0_WAKE
- U_BNO pad 7: SPI1_SCK -> (no net)
- U_BNO pad 8: SPI1_MOSI -> (no net)
- U_BNO pad 9: SPI1_MISO -> BNO_CAP
- U_COAFE pad 1: 3V3_AIR -> GND
- U_COAFE pad 10: CO_RE -> N$32
- U_COAFE pad 11: CO_CE -> CO_VREF
- U_COAFE pad 12: (no net) -> CO_WE
- U_COAFE pad 13: (no net) -> CO_RE
- U_COAFE pad 14: (no net) -> CO_CE
- U_COAFE pad 15: (no net) -> GND
- U_COAFE pad 3: I2CB_SDA -> I2CB_SCL
- U_COAFE pad 4: I2CB_SCL -> I2CB_SDA
- U_COAFE pad 5: GND -> (no net)
- U_COAFE pad 6: CO_AFE_OUT -> 3V3_AIR
- U_COAFE pad 7: N$29 -> GND
- U_COAFE pad 8: N$30 -> CO_AFE_OUT
- U_COAFE pad 9: CO_WE -> N$33
- U_CORE pad 1: VSYS -> N6_PWR_ON
- U_CORE pad 2: GND -> N$18
- U_CORE pad 3: EN_N6 -> GND
- U_CORE pad 4: N$16 -> (no net)
- U_CORE pad 5: N$17 -> GND
- U_CORE pad 6: GND -> N$17
- U_CORE pad 7: (no net) -> VSYS
- U_ENS pad 1: 1V8 -> I2CB_SDA
- U_ENS pad 2: 3V3_AIR -> I2CB_SCL
- U_ENS pad 3: GND -> 3V3_AIR
- U_ENS pad 4: I2CB_SDA -> 1V8_AIR
- U_ENS pad 5: I2CB_SCL -> 3V3_AIR
- U_ENS pad 6: 3V3_AIR -> INT_ENS
- U_ENS pad 7: INT_ENS -> 3V3_AIR
- U_ENS pad 8: 3V3_AIR -> GND
- U_ENS pad 9: (no net) -> GND
- U_GAUGE pad A1: (no net) -> GAUGE_INT_N
- U_GAUGE pad A2: (no net) -> SENT_SDA
- U_GAUGE pad A3: (no net) -> SENT_SCL
- U_GAUGE pad B1: (no net) -> N$7
- U_GAUGE pad B2: (no net) -> GND
- U_GAUGE pad B3: (no net) -> GAUGE_VDD
- U_GAUGE pad C1: (no net) -> GND
- U_GAUGE pad C2: (no net) -> VBAT
- U_GAUGE pad C3: (no net) -> PACKP
- U_HAP pad 1: 3V3_AON -> N$36
- U_HAP pad 10: (no net) -> 3V3_AON
- U_HAP pad 2: GND -> SENT_SCL
- U_HAP pad 4: SENT_SCL -> GND
- U_HAP pad 6: GND -> 3V3_AON
- U_HAP pad 8: LRA_N -> GND
- U_HAP pad 9: (no net) -> LRA_N
- U_MAX pad 1: 1V8 -> (no net)
- U_MAX pad 10: (no net) -> 3V3_CONTACT
- U_MAX pad 11: (no net) -> 1V8
- U_MAX pad 12: (no net) -> GND
- U_MAX pad 13: (no net) -> INT_MAX
- U_MAX pad 2: 3V3_CONTACT -> I2CA_SCL
- U_MAX pad 3: GND -> I2CA_SDA
- U_MAX pad 5: I2CA_SDA -> (no net)
- U_MAX pad 6: I2CA_SCL -> (no net)
- U_MAX pad 7: INT_MAX -> (no net)
- U_MAX pad 9: (no net) -> 3V3_CONTACT
- U_MLX32 pad 1: 3V3_OPTICAL -> I2CA_SDA
- U_MLX32 pad 2: GND -> 3V3_OPTICAL
- U_MLX32 pad 3: I2CA_SDA -> GND
- U_MLX32 pad 5: (no net) -> GND
- U_MLX32 pad 6: (no net) -> GND
- U_MLX42 pad 2: GND -> 3V3_OPTICAL
- U_MLX42 pad 3: 3V3_OPTICAL -> GND
- U_PD pad 1: VBUS_C -> GND
- U_PD pad 11: (no net) -> VBUS_C
- U_PD pad 14: (no net) -> CC2
- U_PD pad 15: (no net) -> CC1
- U_PD pad 18: (no net) -> VBUS_C
- U_PD pad 19: (no net) -> GND
- U_PD pad 2: GND -> N$2
- U_PD pad 22: (no net) -> GND
- U_PD pad 23: (no net) -> PD_VDDD
- U_PD pad 24: (no net) -> N$1
- U_PD pad 25: (no net) -> GND
- U_PD pad 3: CC1 -> (no net)
- U_PD pad 4: CC2 -> (no net)
- U_PD pad 5: N$1 -> N$3
- U_PD pad 6: N$2 -> GND
- U_PD pad 7: N$3 -> (no net)
- U_PD pad 8: N$4 -> (no net)
- U_PD pad 9: PD_FAULT_N -> PD_FAULT
- U_PROT pad 1: PROT_VDD -> (no net)
- U_PROT pad 2: CELL_N -> N$5
- U_PROT pad 3: N$7 -> N$4
- U_PROT pad 4: N$6 -> CELL_N
- U_PROT pad 5: N$5 -> PROT_VDD
- U_PROT pad 6: (no net) -> N$6
- U_RF pad 3: N$24 -> N$27
- U_RF pad 4: N$25 -> N$28
- U_SCD pad 1: 3V3_AIR -> (no net)
- U_SCD pad 10: (no net) -> I2CB_SDA
- U_SCD pad 19: (no net) -> 3V3_AIR
- U_SCD pad 2: GND -> (no net)
- U_SCD pad 20: (no net) -> GND
- U_SCD pad 21: (no net) -> GND
- U_SCD pad 3: I2CB_SDA -> (no net)
- U_SCD pad 4: I2CB_SCL -> (no net)
- U_SCD pad 6: (no net) -> GND
- U_SCD pad 7: (no net) -> 3V3_AIR
- U_SCD pad 9: (no net) -> I2CB_SCL
- U_SGP pad 4: I2CB_SCL -> GND
- U_SGP pad 5: (no net) -> 3V3_AIR
- U_SGP pad 6: (no net) -> I2CB_SCL
- U_SGP pad 7: (no net) -> GND
- U_SHT pad 1: 3V3_AIR -> I2CB_SDA
- U_SHT pad 2: GND -> I2CB_SCL
- U_SHT pad 3: I2CB_SDA -> 3V3_AIR
- U_SHT pad 4: I2CB_SCL -> GND
- U_SYS3V3 pad 1: VSYS -> EN_N6
- U_SYS3V3 pad 2: GND -> N$20
- U_SYS3V3 pad 3: EN_N6 -> GND
- U_SYS3V3 pad 4: N$18 -> (no net)
- U_SYS3V3 pad 5: N$19 -> GND
- U_SYS3V3 pad 6: GND -> N$19
- U_SYS3V3 pad 7: (no net) -> VSYS
- U_TCS pad 1: 3V3_OPTICAL -> 1V8_OPTICAL
- U_TCS pad 2: GND -> I2CA_SCL_1V8
- U_TCS pad 3: I2CB_SDA -> GND
- U_TCS pad 4: I2CB_SCL -> (no net)
- U_TCS pad 5: INT_TCS -> GND
- U_TCS pad 6: (no net) -> 1V8_OPTICAL
- U_TCS pad 7: (no net) -> INT_TCS
- U_TCS pad 8: (no net) -> I2CA_SDA_1V8
- U_TOUCH pad 10: TOUCH_E2 -> TOUCH_E5
- U_TOUCH pad 11: TOUCH_E3 -> TOUCH_E6
- U_TOUCH pad 12: TOUCH_E4 -> TOUCH_E7
- U_TOUCH pad 13: TOUCH_E5 -> TOUCH_E8
- U_TOUCH pad 14: TOUCH_E6 -> (no net)
- U_TOUCH pad 15: TOUCH_E7 -> (no net)
- U_TOUCH pad 16: TOUCH_E8 -> (no net)
- U_TOUCH pad 17: TOUCH_E9 -> TOUCH_RDY_N
- U_TOUCH pad 18: TOUCH_E10 -> SENT_SCL
- U_TOUCH pad 19: TOUCH_E11 -> SENT_SDA
- U_TOUCH pad 2: N$31 -> N$34
- U_TOUCH pad 20: (no net) -> TOUCH_MCLR_N
- U_TOUCH pad 21: (no net) -> GND
- U_TOUCH pad 4: SENT_SDA -> N$35
- U_TOUCH pad 5: SENT_SCL -> TOUCH_E0
- U_TOUCH pad 6: TOUCH_RDY_N -> TOUCH_E1
- U_TOUCH pad 7: TOUCH_MCLR_N -> TOUCH_E2
- U_TOUCH pad 8: TOUCH_E0 -> TOUCH_E3
- U_TOUCH pad 9: TOUCH_E1 -> TOUCH_E4
- U_VL53 pad A1: (no net) -> INT_VL53
- U_VL53 pad A2: (no net) -> LPN_VL53
- U_VL53 pad A3: (no net) -> 1V8_OPTICAL
- U_VL53 pad A4: (no net) -> VL53_MOSI_1V8
- U_VL53 pad A5: (no net) -> VL53_SCLK_1V8
- U_VL53 pad A6: (no net) -> GND
- U_VL53 pad A7: (no net) -> GND
- U_VL53 pad B1: (no net) -> VL53_GPIO2
- U_VL53 pad B4: (no net) -> GND
- U_VL53 pad B7: (no net) -> 1V8_OPTICAL
- U_VL53 pad C1: (no net) -> VL53_SPI_SEL
- U_VL53 pad C2: (no net) -> VL53_NCS_1V8
- U_VL53 pad C3: (no net) -> GND
- U_VL53 pad C4: (no net) -> 3V3_OPTICAL
- U_VL53 pad C5: (no net) -> VL53_MISO_1V8
- U_VL53 pad C6: (no net) -> GND
- U_VL53 pad C7: (no net) -> GND
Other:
- board size 67.9 x 39.9 mm -> 47.7 x 44.7 mm
- copper layers 2 -> 6
